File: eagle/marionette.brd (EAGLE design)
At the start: 139.7 x 76.2 mm, 224 parts, among them J17 MA02-1, J18 MA02-1, J19 MA02-1, J2 SWD, J20 MA02-1, J22 ZX62D-B-5P8, J6 MA03-2W, J8 MA04-2W, Q1 BSS84, U1 STM32F407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

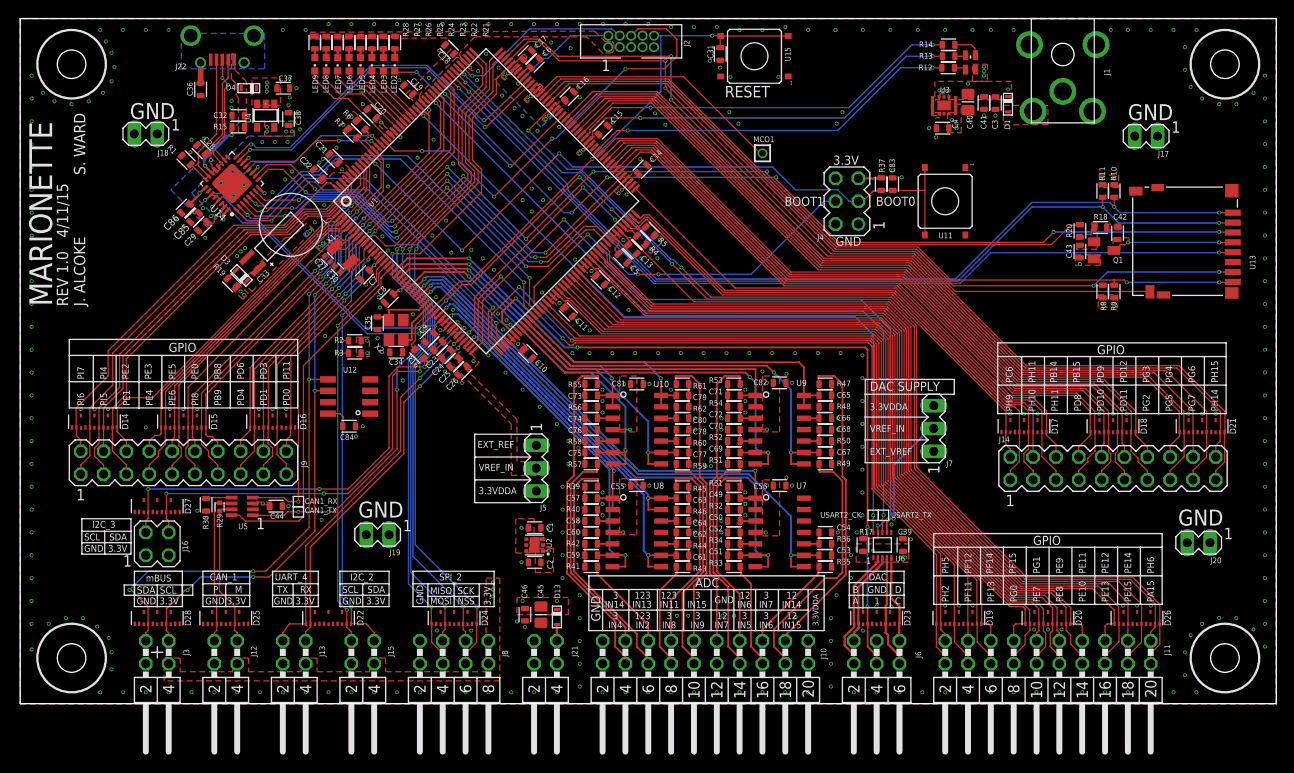
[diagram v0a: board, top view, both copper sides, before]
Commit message: Routed SPI_2 sck and mosi to DAC chip Connected MCO1 to ULPI PHY Cleaned up some
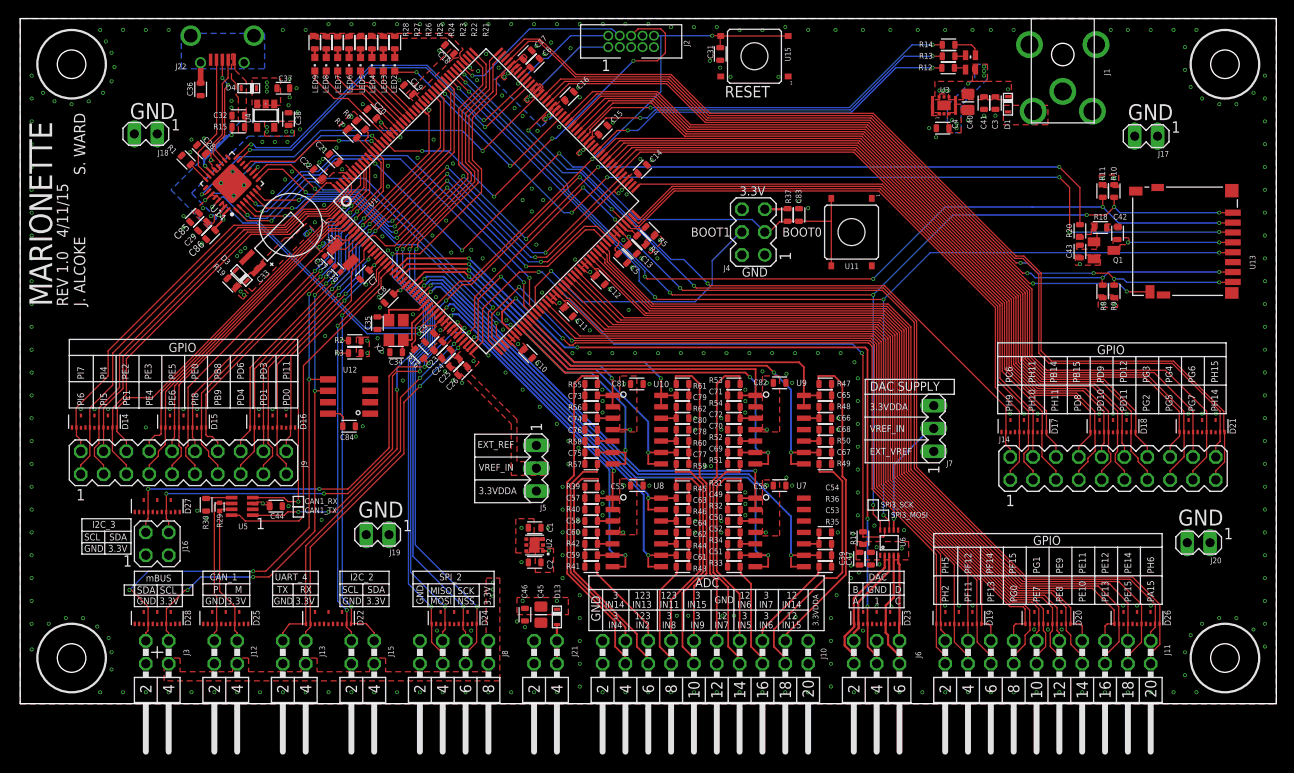
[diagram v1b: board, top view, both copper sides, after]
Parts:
- removed MCO1: TEST-POINT, Tova:2MM-TEST-POINT
- removed USART2_CK: TEST-POINT10MIL-TEST-POINT, Tova:10MIL-TEST-POINT
- added C47: 0.1uF, 10V, rcl_custom:.0603-C
- added SPI3_SCK: TEST-POINT10MIL-TEST-POINT, Tova:10MIL-TEST-POINT
- C39: value 1uF, 10V -> 10uF, 10V
- moved C83 11.0 mm to (86.6, 54.4)
- moved R37 11.0 mm to (85.3, 54.4)
- moved U11 11.0 mm to (92.5, 52.5)
- moved J4 11.0 mm to (81.5, 52.5)
- moved C39 5.06 mm to (93.3, 16.1), turned to 270 degrees
- moved C86 4.04 mm to (21.2, 52.2)
- moved U6 0.80 mm to (96.6, 17.9)
- moved R17 0.76 mm to (93.7, 18.4)
- renumbered USART2_TX to SPI3_MOSI
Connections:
- removed net USART2_CK: U1.151, U6.10, USART2_CK.P$1
- removed net USART2_TX: SPI3_MOSI.P$1, U1.147, U6.8
- net +3.3VDDA: now also C47.1
- net 3.3VDD: no longer U14.14, U14.25, U14.8
- net GND: now also C47.2, U14.14, U14.8
- net MCO1: now also U14.26; no longer MCO1.1
- net PH14: now also D21.P7, J14.20; no longer D21.P8, J14.19
- net PH15: now also D21.P8, J14.19; no longer D21.P7, J14.20
- net SDIO_CK: now also SPI3_MOSI.P$1, U6.8
- net SDIO_D2: now also SPI3_SCK.P$1, U6.10
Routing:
- net USART2_TX: track 83.8 -> 0.00 mm, vias 1 -> 0
- net USART2_CK: track 83.2 -> 0.00 mm, vias 1 -> 0
- net SDIO_CK: track 98.3 -> 126.5 mm, vias 2 -> 4
- net SDIO_D2: track 101.6 -> 129.1 mm, vias 3 -> 6
- net MCO1: track 29.0 -> 45.2 mm, vias 0 -> 2
- net BOOT1: track 43.9 -> 32.6 mm, vias 3 -> 1
- net PH3: track 85.8 -> 76.3 mm
- net BOOT0: track 80.9 -> 71.9 mm
- net 3.3VDD: track 13.9 -> 21.9 mm, vias 51 -> 48
- net PH9: track 60.9 -> 68.7 mm
- net PH10: track 61.8 -> 69.3 mm
- net PH11: track 58.7 -> 66.1 mm
- net PH15: track 105.7 -> 111.0 mm, vias 2 -> 0
- net PH12: track 63.8 -> 68.6 mm
- net PG6: track 90.4 -> 94.7 mm
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
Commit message: Connected PB14 to ULPI refclk MCO1 is connected to a test point again cleaned up GPIO routing
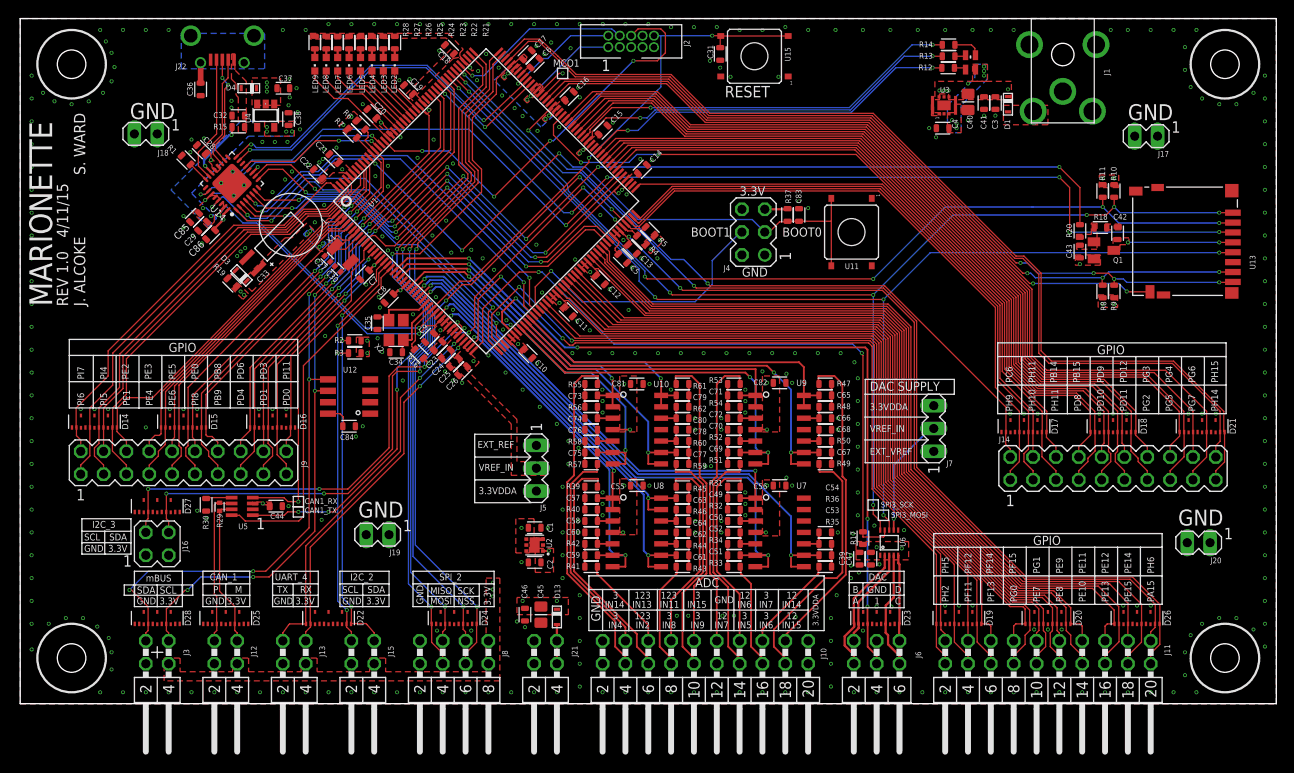
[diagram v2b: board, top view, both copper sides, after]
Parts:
- added MCO1: TEST-POINT10MIL-TEST-POINT, Tova:10MIL-TEST-POINT
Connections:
- new net PD5: U1.147
- new net PD7: LED2.C, U1.151
- net MCO1: now also MCO1.P$1; no longer U14.26
- net PB14: now also U14.26; no longer D17.P8, J14.6
- net PG8: now also D17.P8, J14.6; no longer LED2.C
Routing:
- net PG8: track 25.4 -> 80.8 mm
- net MCO1: track 45.2 -> 3.46 mm, vias 2 -> 0
- net PB14: track 70.2 -> 57.5 mm, vias 0 -> 2
- net PD7: track 0.00 -> 5.22 mm
- net GND: vias 421 -> 418
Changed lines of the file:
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@@
 <attribute name="NAME" x="94.615" y="16.129" size="0.3" layer="33" ratio="15" rot="R270" align="center"/>
 </element>
+<element name="MCO1" library="Tova" package="10MIL-TEST-POINT" value="TEST-POINT10MIL-TEST-POINT" x="60.325" y="70.104"/>
 </elements>
 <signals>
@@
 <wire x1="47.625" y1="61.468" x2="52.705" y2="56.388" width="0.127" layer="16"/>
 <via x="52.705" y="56.388" extent="1-16" drill="0.254"/>
-<wire x1="52.705" y1="56.388" x2="59.182" y2="62.865" width="0.127" layer="1"/>
-<via x="59.182" y="62.865" extent="1-16" drill="0.254"/>
-<wire x1="59.182" y1="62.865" x2="59.563" y2="62.865" width="0.127" layer="16"/>
-<wire x1="59.563" y1="62.865" x2="68.199" y2="71.501" width="0.127" layer="16"/>
+<wire x1="52.705" y1="56.388" x2="58.928" y2="62.611" width="0.127" layer="1"/>
+<via x="58.928" y="62.611" extent="1-16" drill="0.254"/>
+<wire x1="58.928" y1="62.611" x2="59.309" y2="62.611" width="0.127" layer="16"/>
+<wire x1="59.309" y1="62.611" x2="68.199" y2="71.501" width="0.127" layer="16"/>
 <via x="68.199" y="71.501" extent="1-16" drill="0.254"/>
 <wire x1="68.717" y1="75.057" x2="67.945" y2="74.285" width="0.127" layer="1"/>
@@
 <contactref element="U11" pad="1"/>
 <contactref element="C83" pad="2"/>
-<via x="56.896" y="57.277" extent="1-16" drill="0.254"/>
-<via x="58.928" y="57.277" extent="1-16" drill="0.254"/>
-<via x="58.166" y="56.007" extent="1-16" drill="0.254"/>
-<via x="55.88" y="56.007" extent="1-16" drill="0.254"/>
-<via x="56.896" y="54.737" extent="1-16" drill="0.254"/>
 <via x="62.23" y="4.445" extent="1-16" drill="0.254"/>
 <via x="62.23" y="6.985" extent="1-16" drill="0.254"/>
@@
 <via x="92.3925" y="15.367" extent="1-16" drill="0.254"/>
 <via x="98.298" y="19.304" extent="1-16" drill="0.254"/>
+<via x="43.307" y="69.469" extent="1-16" drill="0.254"/>
+<via x="64.516" y="54.356" extent="1-16" drill="0.254"/>
 <wire x1="22.352" y1="57.912" x2="23.553984375" y2="57.8530125" width="0" layer="19" extent="1-1"/>
 </signal>
@@
 <signal name="PB14">
 <contactref element="U1" pad="94"/>
-<wire x1="66.665240625" y1="59.061978125" x2="68.9442625" y2="61.341" width="0.127" layer="1"/>
-<contactref element="J14" pad="6"/>
-<contactref element="D17" pad="P8"/>
-<wire x1="114.133" y1="30.211" x2="114.133" y2="29.885" width="0.127" layer="1"/>
-<wire x1="114.133" y1="29.885" x2="115.189" y2="28.829" width="0.127" layer="1"/>
-<wire x1="115.189" y1="28.829" x2="115.189" y2="27.432" width="0.127" layer="1"/>
-<wire x1="114.133" y1="30.211" x2="114.133" y2="32.552" width="0.127" layer="1"/>
-<wire x1="68.9442625" y1="61.341" x2="92.71" y2="61.341" width="0.127" layer="1"/>
-<wire x1="92.71" y1="61.341" x2="109.474" y2="44.577" width="0.127" layer="1"/>
-<wire x1="109.474" y1="44.577" x2="109.474" y2="37.211" width="0.127" layer="1"/>
-<wire x1="109.474" y1="37.211" x2="114.133" y2="32.552" width="0.127" layer="1"/>
+<contactref element="U14" pad="26"/>
+<wire x1="66.665240625" y1="59.061978125" x2="66.554978125" y2="59.061978125" width="0.127" layer="1"/>
+<wire x1="66.554978125" y1="59.061978125" x2="60.706" y2="53.213" width="0.127" layer="1"/>
+<via x="60.706" y="53.213" extent="1-16" drill="0.254"/>
+<wire x1="60.706" y1="53.213" x2="60.579" y2="53.213" width="0.127" layer="16"/>
+<wire x1="60.579" y1="53.213" x2="49.911" y2="63.881" width="0.127" layer="16"/>
+<wire x1="49.911" y1="63.881" x2="33.655" y2="63.881" width="0.127" layer="16"/>
+<wire x1="33.655" y1="63.881" x2="30.226" y2="60.452" width="0.127" layer="16"/>
+<wire x1="30.226" y1="60.452" x2="25.781" y2="60.452" width="0.127" layer="16"/>
+<wire x1="25.781" y1="60.452" x2="22.733" y2="57.404" width="0.127" layer="16"/>
+<wire x1="22.733" y1="57.404" x2="21.336" y2="57.404" width="0.127" layer="16"/>
+<wire x1="21.336" y1="57.404" x2="20.574" y2="56.642" width="0.127" layer="16"/>
+<wire x1="20.574" y1="56.642" x2="20.066" y2="56.642" width="0.127" layer="16"/>
+<via x="20.066" y="56.642" extent="1-16" drill="0.254"/>
+<wire x1="20.066" y1="56.642" x2="20.57520625" y2="56.642" width="0.127" layer="1"/>
+<wire x1="20.57520625" y1="56.642" x2="20.97304375" y2="57.0398375" width="0.127" layer="1"/>
 </signal>
 <signal name="PC15">
@@
 <wire x1="45.805590625" y1="43.900590625" x2="48.895" y2="46.99" width="0.127" layer="1"/>
 <wire x1="48.895" y1="46.99" x2="50.038" y2="46.99" width="0.127" layer="1"/>
-<wire x1="50.038" y1="46.99" x2="63.627" y2="60.579" width="0.127" layer="1"/>
+<wire x1="50.038" y1="46.99" x2="63.246" y2="60.198" width="0.127" layer="1"/>
+<wire x1="63.246" y1="60.198" x2="63.246" y2="60.706" width="0.127" layer="1"/>
 <wire x1="45.805590625" y1="43.859184375" x2="45.764184375" y2="43.859184375" width="0.127" layer="1"/>
 <wire x1="45.764184375" y1="43.859184375" x2="43.942" y2="42.037" width="0.127" layer="1"/>
@@
 <wire x1="43.561" y1="39.707415625" x2="43.86064375" y2="39.407771875" width="0.127" layer="1"/>
 <wire x1="77.911" y1="74.259" x2="85.411" y2="74.259" width="0.127" layer="1"/>
-<via x="63.627" y="60.579" extent="1-16" drill="0.254"/>
-<wire x1="63.627" y1="60.579" x2="71.247" y2="68.072" width="0.127" layer="16"/>
-<wire x1="71.247" y1="68.072" x2="71.247" y2="74.295" width="0.127" layer="16"/>
+<via x="63.246" y="60.706" extent="1-16" drill="0.254"/>
+<wire x1="63.246" y1="60.706" x2="71.247" y2="68.58" width="0.127" layer="16"/>
+<wire x1="71.247" y1="68.58" x2="71.247" y2="74.295" width="0.127" layer="16"/>
 <wire x1="71.247" y1="74.295" x2="70.485" y2="74.295" width="0.127" layer="16"/>
 <wire x1="77.911" y1="74.259" x2="77.851" y2="74.072" width="0.127" layer="1"/>
@@
 <signal name="MCO1">
 <contactref element="U1" pad="119"/>
-<contactref element="U14" pad="26"/>
-<wire x1="57.82640625" y1="67.9008125" x2="51.435" y2="61.50940625" width="0.127" layer="1"/>
-<wire x1="51.435" y1="61.50940625" x2="51.435" y2="61.468" width="0.127" layer="1"/>
-<via x="51.435" y="61.468" extent="1-16" drill="0.254"/>
-<via x="20.193" y="56.642" extent="1-16" drill="0.254"/>
-<wire x1="20.193" y1="56.642" x2="24.384" y2="60.833" width="0.127" layer="16"/>
-<wire x1="24.384" y1="60.833" x2="30.48" y2="60.833" width="0.127" layer="16"/>
-<wire x1="30.48" y1="60.833" x2="33.401" y2="63.754" width="0.127" layer="16"/>
-<wire x1="33.401" y1="63.754" x2="49.149" y2="63.754" width="0.127" layer="16"/>
-<wire x1="49.149" y1="63.754" x2="51.435" y2="61.468" width="0.127" layer="16"/>
-<wire x1="20.193" y1="56.642" x2="20.57520625" y2="56.642" width="0.127" layer="1"/>
-<wire x1="20.57520625" y1="56.642" x2="20.97304375" y2="57.0398375" width="0.127" layer="1"/>
+<contactref element="MCO1" pad="P$1"/>
+<wire x1="57.82640625" y1="67.9008125" x2="57.82640625" y2="67.98640625" width="0.127" layer="1"/>
+<wire x1="57.82640625" y1="67.98640625" x2="59.944" y2="70.104" width="0.127" layer="1"/>
+<wire x1="59.944" y1="70.104" x2="60.325" y2="70.104" width="0.127" layer="1"/>
 </signal>
 <signal name="SD_DETECT">
@@
 <wire x1="114.173" y1="37.084" x2="127.381" y2="37.084" width="0.127" layer="1"/>
 </signal>
-<signal name="PG8">
-<contactref element="U1" pad="112"/>
-<contactref element="LED2" pad="C"/>
-<wire x1="60.30128125" y1="65.425940625" x2="54.692340625" y2="59.817" width="0.127" layer="1"/>
-<wire x1="54.692340625" y1="59.817" x2="54.483" y2="59.817" width="0.127" layer="1"/>
-<via x="54.483" y="59.817" extent="1-16" drill="0.254"/>
-<wire x1="54.483" y1="59.817" x2="44.069" y2="70.231" width="0.127" layer="16"/>
-<via x="44.069" y="70.231" extent="1-16" drill="0.254"/>
-<wire x1="44.069" y1="70.231" x2="41.656" y2="70.231" width="0.127" layer="1"/>
-<wire x1="41.656" y1="70.231" x2="41.656" y2="70.37" width="0.127" layer="1"/>
-</signal>
 <signal name="PG9">
 <contactref element="U1" pad="152"/>
@@
 </polygon>
 </signal>
+<signal name="PG8">
+<contactref element="U1" pad="112"/>
+<contactref element="J14" pad="6"/>
+<contactref element="D17" pad="P8"/>
+<wire x1="60.30128125" y1="65.425940625" x2="60.30128125" y2="65.38128125" width="0.127" layer="1"/>
+<wire x1="60.30128125" y1="65.38128125" x2="59.309" y2="64.389" width="0.127" layer="1"/>
+<wire x1="59.309" y1="64.389" x2="59.309" y2="63.246" width="0.127" layer="1"/>
+<wire x1="59.309" y1="63.246" x2="62.357" y2="60.198" width="0.127" layer="1"/>
+<via x="62.357" y="60.198" extent="1-16" drill="0.254"/>
+<wire x1="62.357" y1="60.198" x2="67.691" y2="60.198" width="0.127" layer="16"/>
+<wire x1="67.691" y1="60.198" x2="68.58" y2="61.087" width="0.127" layer="16"/>
+<wire x1="68.58" y1="61.087" x2="70.993" y2="61.087" width="0.127" layer="16"/>
+<via x="70.993" y="61.087" extent="1-16" drill="0.254"/>
+<wire x1="70.993" y1="61.087" x2="92.964" y2="61.087" width="0.127" layer="1"/>
+<wire x1="92.964" y1="61.087" x2="109.474" y2="44.577" width="0.127" layer="1"/>
+<wire x1="109.474" y1="44.577" x2="109.474" y2="37.211" width="0.127" layer="1"/>
+<wire x1="109.474" y1="37.211" x2="114.173" y2="32.512" width="0.127" layer="1"/>
+<wire x1="114.173" y1="32.512" x2="114.173" y2="30.251" width="0.127" layer="1"/>
+<wire x1="114.173" y1="30.251" x2="114.133" y2="30.211" width="0.127" layer="1"/>
+<wire x1="114.133" y1="30.211" x2="114.133" y2="29.631" width="0.127" layer="1"/>
+<wire x1="114.133" y1="29.631" x2="115.189" y2="28.575" width="0.127" layer="1"/>
+<wire x1="115.189" y1="28.575" x2="115.189" y2="27.432" width="0.127" layer="1"/>
+</signal>
+<signal name="PD5">
+<contactref element="U1" pad="147"/>
+</signal>
+<signal name="PD7">
+<contactref element="U1" pad="151"/>
+<contactref element="LED2" pad="C"/>
+<wire x1="44.037825" y1="66.133046875" x2="44.037825" y2="66.198175" width="0.127" layer="1"/>
+<wire x1="44.037825" y1="66.198175" x2="41.656" y2="68.58" width="0.127" layer="1"/>
+<wire x1="41.656" y1="68.58" x2="41.656" y2="70.37" width="0.127" layer="1"/>
+</signal>
 </signals>

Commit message: Changed names of nets: 	SDIO_CK --> SDIO_CK-SPI3_MOSI 	SDIO_D2 --> SDIO_D2-SPI3_SCK
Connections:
- net SDIO_CK renamed SDIO_CK-SPI3_MOSI
- net SDIO_D2 renamed SDIO_D2-SPI3_SCK
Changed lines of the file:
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@@
 <wire x1="22.352" y1="57.912" x2="23.553984375" y2="57.8530125" width="0" layer="19" extent="1-1"/>
 </signal>
-<signal name="SDIO_CK">
+<signal name="SDIO_CK-SPI3_MOSI">
 <contactref element="U1" pad="141"/>
 <contactref element="U13" pad="P5"/>
@@
 <wire x1="102.87" y1="55.245" x2="112.522" y2="55.245" width="0.127" layer="16"/>
 </signal>
-<signal name="SDIO_D2">
+<signal name="SDIO_D2-SPI3_SCK">
 <contactref element="U1" pad="139"/>
 <contactref element="U13" pad="P1"/>
